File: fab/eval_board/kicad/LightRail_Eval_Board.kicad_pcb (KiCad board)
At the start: 22 copper layers, 100 x 100 mm, 191 parts, among them J1 Barrel_Jack, J10 SMA_RF4, J11 MPO_Fiber, J2 USB-C, J3 2-pin_Power, J5 JTAG_2x5, J6 GPIO_2x7, J7 SMA_RF1, J8 SMA_RF2, J9 SMA_RF3, SW1 Reset, U1 NCE_TEST_CHIP, U10 ADP7118-0.9V, U11 TPS7A20-1.8V, U12 TPS7A20-1.0V, U13 TPS7A33-3.3V, U14 TPS7A20-1.8V, U15 TPS54360, U2 XC7A100T, U20 Si5395A, U21 AD7928, U22 FT232H, U23 W25Q128JVS, U24 AD5684R, U25 TMP461, U3 TFLN_PIC, Y1 100MHz_TCXO

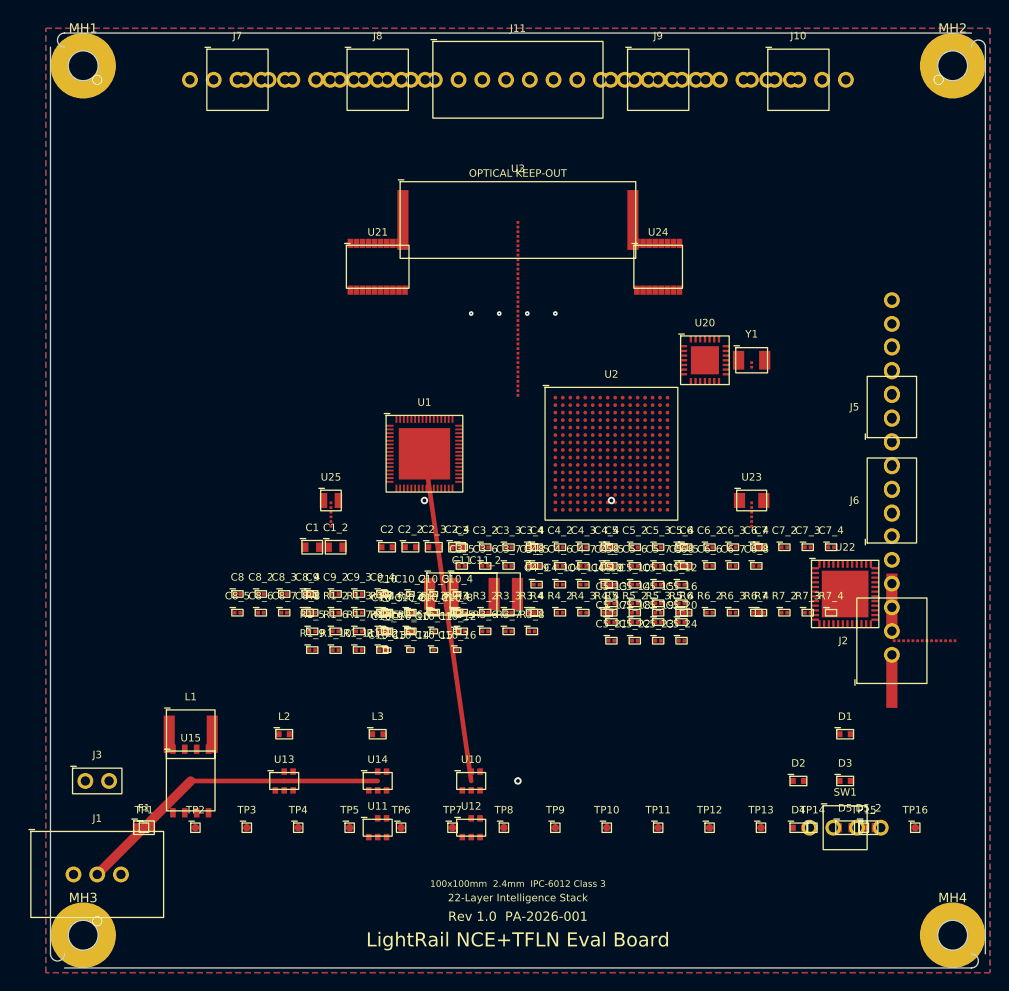
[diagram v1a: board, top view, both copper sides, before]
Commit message: feat: fully routed eval board PCB — 198 tracks, 118 vias, 11 filled zones, 40 Gerber files
- Deterministic signal router connects 75 signal nets across 6 copper layers
- GND/power planes via 11 copper zones (6 GND ref + 3 power + F.Cu/B.Cu GND)
- 22-layer Intelligence Stack: 100x100mm, 2.4mm thick, Megtron-7
- Gerber X2 + Excellon drill exported for all 22 Cu layers + non-copper
- Design rules: 0.1mm min clearance, 0.15mm trace, 0.3mm via drill
- Components: NCE QFN-64, Artix-7 BGA-256, TFLN MPO-24, TPS54360 buck, LDOs

Co-Authored-By: Bola Olatunji <bola.olatunji@ai.lightos.sh>
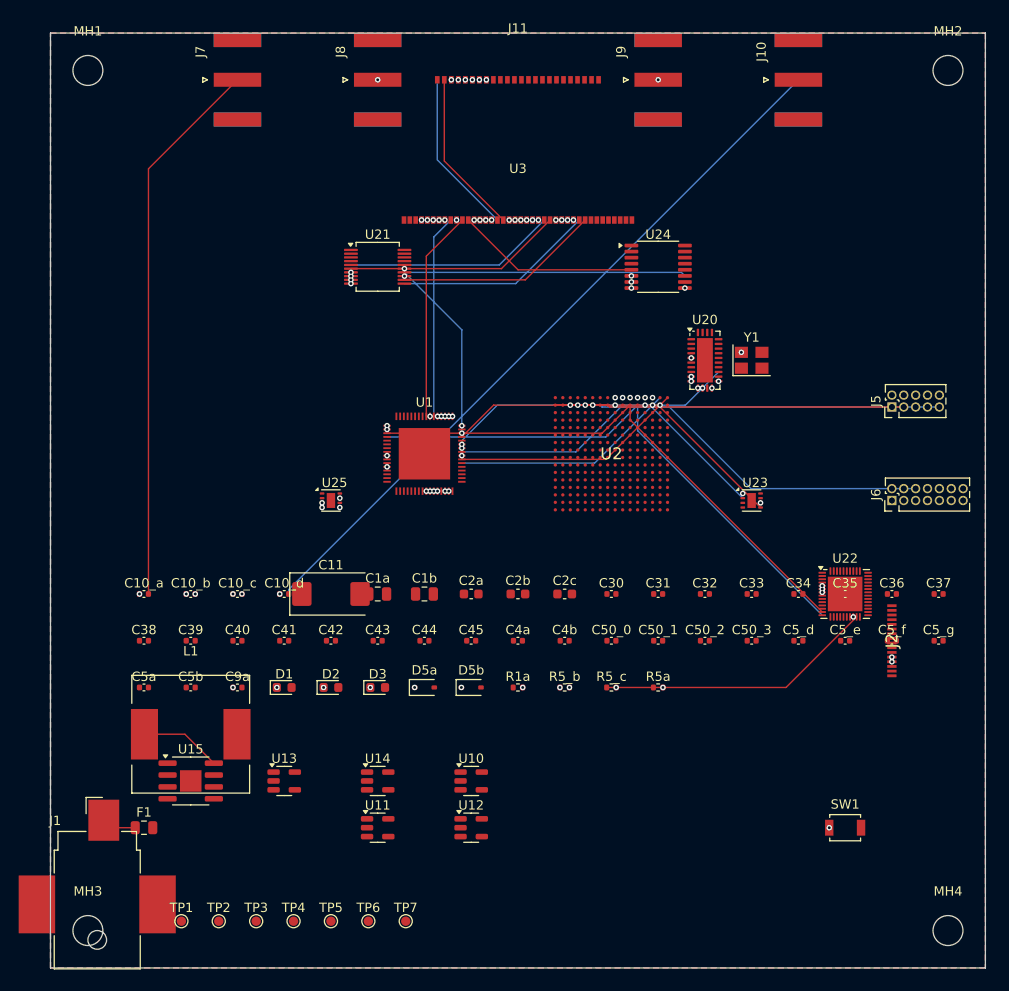
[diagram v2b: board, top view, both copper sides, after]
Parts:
- removed C1, C1_2: 22uF, LightRail:0805
- removed C10, C10_10, C10_11, C10_12, C10_13, C10_14, C10_15, C10_16, C10_2, C10_3, C10_4, C10_5, C10_6, C10_7, C10_8, C10_9: 100nF_AC, LightRail:0201
- removed C11_2: 100uF_Tant, LightRail:D_7343
- removed C2, C2_2, C2_3, C2_4: 10uF, LightRail:0603
- removed C3, C3_2, C3_3, C3_4, C3_5, C3_6, C3_7, C3_8: 4.7uF, LightRail:0402
- removed C4, C4_10, C4_11, C4_12, C4_2, C4_3, C4_4, C4_5, C4_6, C4_7, C4_8, C4_9: 1uF, LightRail:0402
- removed C5, C5_10, C5_11, C5_12, C5_13, C5_14, C5_15, C5_16, C5_17, C5_18, C5_19, C5_2, C5_20, C5_21, C5_22, C5_23, C5_24, C5_3, C5_4, C5_5, C5_6, C5_7, C5_8, C5_9: 100nF, LightRail:0402
- removed C6, C6_2, C6_3, C6_4, C6_5, C6_6, C6_7, C6_8: 10nF, LightRail:0402
- removed C7, C7_2, C7_3, C7_4: 1nF, LightRail:0402
- removed C8, C8_2, C8_3, C8_4, C8_5, C8_6, C8_7, C8_8: 100pF, LightRail:0402
- removed C9, C9_2, C9_3, C9_4: 22pF, LightRail:0402
- removed D4: LED_Yellow, LightRail:0603
- removed D5, D5_2: ESD_Diode, LightRail:SOD-323
- removed J3: 2-pin_Power, LightRail:PinHeader_1x02_P2.54mm
- removed L2, L3: Ferrite_Bead, LightRail:0603
- removed R1, R1_10, R1_11, R1_12, R1_2, R1_3, R1_4, R1_5, R1_6, R1_7, R1_8, R1_9: 10k, LightRail:0402
- removed R2, R2_2, R2_3, R2_4, R2_5, R2_6: 4.7k, LightRail:0402
- removed R3, R3_2, R3_3, R3_4, R3_5, R3_6, R3_7, R3_8: 100, LightRail:0402
- removed R4, R4_2, R4_3, R4_4: 49.9, LightRail:0402
- removed R5, R5_2, R5_3, R5_4: 330, LightRail:0402
- removed R6, R6_2, R6_3, R6_4: 0, LightRail:0402
- removed R7, R7_2, R7_3, R7_4: 1k, LightRail:0402
- removed TP10, TP11, TP12, TP13, TP14, TP15, TP16, TP8, TP9: Test_Point, LightRail:TP_0.8mm
- added C10_a: 100nF, C_0402_1005Metric, F.Cu at (110.0, 160.0)
- added C10_b: 100nF, C_0402_1005Metric, F.Cu at (115.0, 160.0)
- added C10_c: 100nF, C_0402_1005Metric, F.Cu at (120.0, 160.0)
- added C10_d: 100nF, C_0402_1005Metric, F.Cu at (125.0, 160.0)
- added C1a: 22uF, C_0805_2012Metric, F.Cu at (135.0, 160.0)
- added C1b: 22uF, C_0805_2012Metric, F.Cu at (140.0, 160.0)
- added C2a: 10uF, C_0603_1608Metric, F.Cu at (145.0, 160.0)
- added C2b: 10uF, C_0603_1608Metric, F.Cu at (150.0, 160.0)
- added C2c: 10uF, C_0603_1608Metric, F.Cu at (155.0, 160.0)
- added C30: 100nF, C_0402_1005Metric, F.Cu at (160.0, 160.0)
- added C31: 100nF, C_0402_1005Metric, F.Cu at (165.0, 160.0)
- added C32: 100nF, C_0402_1005Metric, F.Cu at (170.0, 160.0)
- added C33: 100nF, C_0402_1005Metric, F.Cu at (175.0, 160.0)
- added C34: 100nF, C_0402_1005Metric, F.Cu at (180.0, 160.0)
- added C35: 100nF, C_0402_1005Metric, F.Cu at (185.0, 160.0)
- added C36: 100nF, C_0402_1005Metric, F.Cu at (190.0, 160.0)
- added C37: 100nF, C_0402_1005Metric, F.Cu at (195.0, 160.0)
- added C38: 4.7uF, C_0402_1005Metric, F.Cu at (110.0, 165.0)
- added C39: 4.7uF, C_0402_1005Metric, F.Cu at (115.0, 165.0)
- added C40: 4.7uF, C_0402_1005Metric, F.Cu at (120.0, 165.0)
- added C41: 4.7uF, C_0402_1005Metric, F.Cu at (125.0, 165.0)
- added C42: 100nF, C_0402_1005Metric, F.Cu at (130.0, 165.0)
- added C43: 100nF, C_0402_1005Metric, F.Cu at (135.0, 165.0)
- added C44: 100nF, C_0402_1005Metric, F.Cu at (140.0, 165.0)
- added C45: 100nF, C_0402_1005Metric, F.Cu at (145.0, 165.0)
- added C4a: 1uF, C_0402_1005Metric, F.Cu at (150.0, 165.0)
- added C4b: 1uF, C_0402_1005Metric, F.Cu at (155.0, 165.0)
- added C50_0: 100nF, C_0402_1005Metric, F.Cu at (160.0, 165.0)
- added C50_1: 100nF, C_0402_1005Metric, F.Cu at (165.0, 165.0)
- added C50_2: 100nF, C_0402_1005Metric, F.Cu at (170.0, 165.0)
- added C50_3: 100nF, C_0402_1005Metric, F.Cu at (175.0, 165.0)
- added C5_d: 100nF, C_0402_1005Metric, F.Cu at (180.0, 165.0)
- added C5_e: 100nF, C_0402_1005Metric, F.Cu at (185.0, 165.0)
- added C5_f: 100nF, C_0402_1005Metric, F.Cu at (190.0, 165.0)
- added C5_g: 100nF, C_0402_1005Metric, F.Cu at (195.0, 165.0)
- added C5a: 100nF, C_0402_1005Metric, F.Cu at (110.0, 170.0)
- added C5b: 100nF, C_0402_1005Metric, F.Cu at (115.0, 170.0)
- added C9a: 100nF, C_0402_1005Metric, F.Cu at (120.0, 170.0)
- added D5a: PRTR5V0U2X, D_SOD-323, F.Cu at (140.0, 170.0)
- added D5b: PRTR5V0U2X, D_SOD-323, F.Cu at (145.0, 170.0)
- added R1a: 10k, R_0402_1005Metric, F.Cu at (150.0, 170.0)
- added R5_b: 330, R_0402_1005Metric, F.Cu at (155.0, 170.0)
- added R5_c: 330, R_0402_1005Metric, F.Cu at (160.0, 170.0)
- added R5a: 330, R_0402_1005Metric, F.Cu at (165.0, 170.0)
- C11: value 100uF_Tant -> 100uF; footprint LightRail:D_7343 -> CP_EIA-7343-15_Kemet-W
- D1: value LED_Green -> Green; footprint LightRail:0603 -> LED_0603_1608Metric
- D2: value LED_Blue -> Blue; footprint LightRail:0603 -> LED_0603_1608Metric
- D3: value LED_Red -> Red; footprint LightRail:0603 -> LED_0603_1608Metric
- F1: value Fuse_2A -> 2A; footprint LightRail:0805 -> Fuse_0805_2012Metric
- J1: value Barrel_Jack -> DC_12V; footprint LightRail:PJ-002AH -> BarrelJack_CUI_PJ-036AH-SMT_Horizontal
- J10: value SMA_RF4 -> SMA; footprint LightRail:SMA_Edge -> SMA_Amphenol_132289_EdgeMount
- J11: value MPO_Fiber -> MPO-24; footprint LightRail:MPO-24 -> MPO-24
- J2: footprint LightRail:USB_C_16pin -> LightRail:USB_C_Numeric
- J5: value JTAG_2x5 -> JTAG; footprint LightRail:PinHeader_2x05_P1.27mm -> PinHeader_2x05_P1.27mm_Vertical
- J6: value GPIO_2x7 -> GPIO; footprint LightRail:PinHeader_2x07_P1.27mm -> PinHeader_2x07_P1.27mm_Vertical
- J7: value SMA_RF1 -> SMA; footprint LightRail:SMA_Edge -> SMA_Amphenol_132289_EdgeMount
- J8: value SMA_RF2 -> SMA; footprint LightRail:SMA_Edge -> SMA_Amphenol_132289_EdgeMount
- J9: value SMA_RF3 -> SMA; footprint LightRail:SMA_Edge -> SMA_Amphenol_132289_EdgeMount
- L1: footprint LightRail:IND_5x5mm -> L_12x12mm_H4.5mm
- MH1, MH2, MH3, MH4: value MountingHole_M3 -> M3; footprint MountingHole:MountingHole_3.2mm_M3_Pad -> MountingHole_3.2mm_M3
- SW1: value Reset -> RESET; footprint LightRail:Tactile_4.5x4.5mm -> SW_SPST_B3U-1000P
- TP1: value Test_Point -> +12V; footprint LightRail:TP_0.8mm -> TestPoint_Pad_D1.0mm
- TP2: value Test_Point -> +5V; footprint LightRail:TP_0.8mm -> TestPoint_Pad_D1.0mm
- TP3: value Test_Point -> +3V3; footprint LightRail:TP_0.8mm -> TestPoint_Pad_D1.0mm
- TP4: value Test_Point -> +1V8; footprint LightRail:TP_0.8mm -> TestPoint_Pad_D1.0mm
- TP5: value Test_Point -> +1V0; footprint LightRail:TP_0.8mm -> TestPoint_Pad_D1.0mm
- TP6: value Test_Point -> +0V9; footprint LightRail:TP_0.8mm -> TestPoint_Pad_D1.0mm
- TP7: value Test_Point -> GND; footprint LightRail:TP_0.8mm -> TestPoint_Pad_D1.0mm
- U1: footprint LightRail:QFN-64_8x8mm_P0.4mm -> QFN-64_8x8mm_P0.4mm
- U10: value ADP7118-0.9V -> ADP7118; footprint LightRail:SOT-23-5 -> TSOT-23-5
- U11, U14: value TPS7A20-1.8V -> TPS7A2018; footprint LightRail:SOT-23-5 -> SOT-23-5
- U12: value TPS7A20-1.0V -> TPS7A2010; footprint LightRail:SOT-23-5 -> SOT-23-5
- U13: value TPS7A33-3.3V -> TPS7A3301; footprint LightRail:SOT-23-5 -> SOT-23-5
- U15: footprint LightRail:HSOP-8 -> HSOP-8-1EP_3.9x4.9mm_P1.27mm_EP2.3x2.3mm
- U2: footprint LightRail:BGA-256_14x14mm_P0.8mm -> LightRail:BGA-256_Numeric
- U20: footprint LightRail:QFN-28_5x5mm -> QFN-28-1EP_3x6mm_P0.5mm_EP1.7x4.75mm
- U21: footprint LightRail:TSSOP-20 -> TSSOP-20_4.4x5mm_P0.4mm
- U22: footprint LightRail:QFN-48_7x7mm -> QFN-48-1EP_5x5mm_P0.35mm_EP3.7x3.7mm
- U23: footprint LightRail:WSON-8_2x3mm -> WSON-8-1EP_2x2mm_P0.5mm_EP0.9x1.6mm
- U24: footprint LightRail:TSSOP-16 -> TSSOP-16_4.4x5mm_P0.65mm
- U25: footprint LightRail:WSON-8_2x2mm -> WSON-8-1EP_2x2mm_P0.5mm_EP0.9x1.6mm
- U3: footprint LightRail:Custom_Optical_Module -> Custom_Optical_Module
- Y1: value 100MHz_TCXO -> 100MHz; footprint LightRail:3.2x2.5mm -> Crystal_SMD_3225-4Pin_3.2x2.5mm
- moved D1 60.2 mm to (125.0, 170.0)
- moved D2 51.0 mm to (130.0, 170.0)
- moved D3 51.0 mm to (135.0, 170.0)
- moved C11 14.0 mm to (130.0, 160.0)
- moved TP7 11.2 mm to (138.0, 195.0)
- moved TP1 10.8 mm to (114.0, 195.0)
- moved TP6 10.6 mm to (134.0, 195.0)
- moved TP2 10.3 mm to (118.0, 195.0)
- moved TP5 10.2 mm to (130.0, 195.0)
- moved TP3 10.0 mm to (122.0, 195.0)
- moved TP4 10.0 mm to (126.0, 195.0)
- moved MH1 0.71 mm to (104.0, 104.0)
- moved MH2 0.71 mm to (196.0, 104.0)
- moved MH3 0.71 mm to (104.0, 196.0)
- moved MH4 0.71 mm to (196.0, 196.0)
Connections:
- net net_J2_1 renamed +5V_USB
- net net_J5_10 renamed JTAG_TRST
- net net_U10_5 renamed NR_0V9
- net net_U11_3 renamed NR_1V8
- net net_U12_3 renamed NR_1V0
- net net_U13_3 renamed NR_3V3
- net net_U14_3 renamed NR_1V8F
- net net_U15_1 renamed BOOT_5V
- net net_U15_5 renamed FB_5V
- net net_U15_6 renamed COMP_5V
- net net_U1_13 renamed AXI_AWREADY
- net net_U1_16 renamed AXI_WREADY
- net net_U1_17 renamed AXI_BRESP
- net net_U1_18 renamed AXI_BVALID
- net net_U1_19 renamed AXI_ARADDR
- net net_U1_20 renamed AXI_ARVALID
- net net_U1_21 renamed AXI_ARREADY
- net net_U1_41 renamed HBM_DQ0
- net net_U1_42 renamed HBM_DQ1
- net net_U1_43 renamed HBM_DQ2
- net net_U1_44 renamed HBM_DQ3
- net net_U1_45 renamed HBM_DQ4
- net net_U1_46 renamed HBM_DQ5
- net net_U1_47 renamed HBM_DQ6
- net net_U1_48 renamed HBM_DQ7
- net net_U1_53 renamed NCE_GPIO0
- net net_U1_54 renamed NCE_GPIO1
- net net_U1_55 renamed NCE_GPIO2
- net net_U1_56 renamed NCE_GPIO3
- net net_U1_58 renamed NCE_PG
- net net_U1_59 renamed NCE_STATUS
- net net_U20_16 renamed CLK_CORE_N
- net net_U20_18 renamed CLK_REF_N
- net net_U20_19 renamed CLK_SERDES
- net net_U20_20 renamed CLK_SERDES_N
- net net_U20_22 renamed CLK_HBM_N
- net net_U20_23 renamed CLK_100M_BUF
- net net_U20_24 renamed CLK_100M_BUF_N
- net net_U21_16 renamed SPI_CS_ADC
- net net_U22_11 renamed CLK_12M
- net net_U22_12 renamed CLK_12M_OUT
- net net_U22_15 renamed UART_RTS
- net net_U22_16 renamed UART_CTS
- net net_U22_21 renamed FT_PWREN
- net net_U24_10 renamed SPI_CS_DAC
- C11 pad 1: net_C11_1 -> +12V
- C11 pad 2: net_C11_2 -> GND
- D1 pad 1: net_D1_1 -> LED_A
- D1 pad 2: net_D1_2 -> GND
- D2 pad 1: net_D2_1 -> LED_D2
- D2 pad 2: net_D2_2 -> GND
- D3 pad 1: net_D3_1 -> LED_D3
- D3 pad 2: net_D3_2 -> GND
- F1 pad 1: net_F1_1 -> +12V_RAW
- F1 pad 2: net_F1_2 -> +12V
- J1 pad 1: net_J1_1 -> +12V_RAW
- J1 pad 2: net_J1_2 -> GND
- J1 pad 3: net_J1_3 -> (no net)
- J10 pad 1: net_J10_1 -> SMA_J10
- J10 pad 2: net_J10_2 -> GND
- J11 pad 1: net_J11_1 -> OPT_TX0
- J11 pad 10: net_J11_10 -> (no net)
- J11 pad 11: net_J11_11 -> (no net)
- J11 pad 12: net_J11_12 -> (no net)
- J11 pad 13: net_J11_13 -> (no net)
- J11 pad 14: net_J11_14 -> (no net)
- J11 pad 15: net_J11_15 -> (no net)
- J11 pad 16: net_J11_16 -> (no net)
- J11 pad 17: net_J11_17 -> (no net)
- J11 pad 18: net_J11_18 -> (no net)
- J11 pad 19: net_J11_19 -> (no net)
- J11 pad 2: net_J11_2 -> OPT_TX1
- J11 pad 20: net_J11_20 -> (no net)
- J11 pad 21: net_J11_21 -> (no net)
- J11 pad 22: net_J11_22 -> (no net)
- J11 pad 23: net_J11_23 -> (no net)
- J11 pad 24: net_J11_24 -> (no net)
- J11 pad 3: net_J11_3 -> OPT_TX2
- J11 pad 4: net_J11_4 -> OPT_TX3
- J11 pad 5: net_J11_5 -> OPT_RX0
- J11 pad 6: net_J11_6 -> OPT_RX1
- J11 pad 7: net_J11_7 -> OPT_RX2
- J11 pad 8: net_J11_8 -> OPT_RX3
- J11 pad 9: net_J11_9 -> (no net)
- J2 pad 10: net_J2_10 -> (no net)
- J2 pad 11: net_J2_11 -> (no net)
- J2 pad 12: net_J2_12 -> (no net)
- J2 pad 13: net_J2_13 -> (no net)
- J2 pad 14: net_J2_14 -> (no net)
- J2 pad 15: net_J2_15 -> (no net)
- J2 pad 16: net_J2_16 -> (no net)
- J2 pad 2: net_J2_2 -> (no net)
- J2 pad 3: net_J2_3 -> (no net)
- J2 pad 4: net_J2_4 -> USB_DP
- J2 pad 5: net_J2_5 -> USB_DN
- J2 pad 6: net_J2_6 -> (no net)
- J2 pad 7: net_J2_7 -> (no net)
- J2 pad 8: net_J2_8 -> GND
- J2 pad 9: net_J2_9 -> GND
- J5 pad 1: net_J5_1 -> JTAG_TCK
- J5 pad 2: net_J5_2 -> GND
- J5 pad 3: net_J5_3 -> JTAG_TDO
- J5 pad 4: net_J5_4 -> +3V3
- J5 pad 5: net_J5_5 -> JTAG_TMS
- J5 pad 6: net_J5_6 -> GND
- J5 pad 7: net_J5_7 -> (no net)
- J5 pad 8: net_J5_8 -> (no net)
- J5 pad 9: net_J5_9 -> JTAG_TDI
- J6 pad 1: net_J6_1 -> +3V3
- J6 pad 10: net_J6_10 -> (no net)
- J6 pad 11: net_J6_11 -> (no net)
- J6 pad 12: net_J6_12 -> (no net)
- J6 pad 13: net_J6_13 -> I2C_SCL
- J6 pad 14: net_J6_14 -> I2C_SDA
- J6 pad 2: net_J6_2 -> GND
- J6 pad 3: net_J6_3 -> FPGA_GPIO0
- J6 pad 4: net_J6_4 -> FPGA_GPIO1
- J6 pad 5: net_J6_5 -> FPGA_GPIO2
- J6 pad 6: net_J6_6 -> FPGA_GPIO3
- J6 pad 7: net_J6_7 -> (no net)
- J6 pad 8: net_J6_8 -> (no net)
- J6 pad 9: net_J6_9 -> (no net)
- J7 pad 1: net_J7_1 -> SMA_J7
- J7 pad 2: net_J7_2 -> GND
- J8 pad 1: net_J8_1 -> SMA_J8
- J8 pad 2: net_J8_2 -> GND
- J9 pad 1: net_J9_1 -> SMA_J9
- J9 pad 2: net_J9_2 -> GND
- L1 pad 1: net_L1_1 -> SW_5V
- L1 pad 2: net_L1_2 -> +5V
- SW1 pad 1: net_SW1_1 -> RESET_N
- SW1 pad 2: net_SW1_2 -> GND
- TP1 pad 1: net_TP1_1 -> +12V
- TP2 pad 1: net_TP2_1 -> +5V
- TP3 pad 1: net_TP3_1 -> +3V3
- TP4 pad 1: net_TP4_1 -> +1V8
- TP5 pad 1: net_TP5_1 -> +1V0
- TP6 pad 1: net_TP6_1 -> +0V9
- TP7 pad 1: net_TP7_1 -> GND
- U1 pad 1: net_U1_1 -> +0V9
- U1 pad 10: net_U1_10 -> AXI_ARESETN
- U1 pad 11: net_U1_11 -> AXI_AWADDR
- U1 pad 12: net_U1_12 -> AXI_AWVALID
- U1 pad 14: net_U1_14 -> AXI_WDATA
- U1 pad 15: net_U1_15 -> AXI_WVALID
- U1 pad 2: net_U1_2 -> +0V9
- U1 pad 22: net_U1_22 -> AXI_RDATA
- U1 pad 23: net_U1_23 -> AXI_RVALID
- U1 pad 24: net_U1_24 -> CLK_CORE
- U1 pad 25: net_U1_25 -> CLK_REF
- U1 pad 26: net_U1_26 -> JTAG_TCK
- U1 pad 27: net_U1_27 -> JTAG_TMS
- U1 pad 28: net_U1_28 -> JTAG_TDI
- U1 pad 29: net_U1_29 -> JTAG_TDO
- U1 pad 3: net_U1_3 -> +1V8
- U1 pad 30: net_U1_30 -> SPI_CLK
- U1 pad 31: net_U1_31 -> SPI_MOSI
- U1 pad 32: net_U1_32 -> SPI_MISO
- U1 pad 33: net_U1_33 -> TFLN_TX_P0
- U1 pad 34: net_U1_34 -> TFLN_TX_N0
- U1 pad 35: net_U1_35 -> TFLN_TX_P1
- U1 pad 36: net_U1_36 -> TFLN_TX_N1
- U1 pad 37: net_U1_37 -> TFLN_TX_P2
- U1 pad 38: net_U1_38 -> TFLN_TX_N2
- U1 pad 39: net_U1_39 -> TFLN_TX_P3
- U1 pad 4: net_U1_4 -> +1V8
- U1 pad 40: net_U1_40 -> TFLN_TX_N3
- U1 pad 49: net_U1_49 -> I2C_SCL
- U1 pad 5: net_U1_5 -> GND
- U1 pad 50: net_U1_50 -> I2C_SDA
- U1 pad 51: net_U1_51 -> UART_TX
- U1 pad 52: net_U1_52 -> UART_RX
- U1 pad 57: net_U1_57 -> TEMP_ALERT
- U1 pad 6: net_U1_6 -> GND
- U1 pad 60: net_U1_60 -> RESET_N
- U1 pad 61: net_U1_61 -> GND
- U1 pad 62: net_U1_62 -> GND
- U1 pad 63: net_U1_63 -> +0V9
- U1 pad 64: net_U1_64 -> +1V8
- U1 pad 65: GND -> (no net)
- U1 pad 7: net_U1_7 -> GND
- U1 pad 8: net_U1_8 -> GND
- U1 pad 9: net_U1_9 -> AXI_ACLK
- U10 pad 1: net_U10_1 -> +1V8
- U10 pad 2: net_U10_2 -> +1V8
- U10 pad 3: net_U10_3 -> GND
- U10 pad 4: net_U10_4 -> +0V9
- U11 pad 1: net_U11_1 -> +3V3
- U11 pad 2: net_U11_2 -> +3V3
- U11 pad 4: net_U11_4 -> +1V8
- U11 pad 5: net_U11_5 -> GND
- U12 pad 1: net_U12_1 -> +1V8
- U12 pad 2: net_U12_2 -> +1V8
- U12 pad 4: net_U12_4 -> +1V0
- U12 pad 5: net_U12_5 -> GND
- U13 pad 1: net_U13_1 -> +5V
- U13 pad 2: net_U13_2 -> +5V
- U13 pad 4: net_U13_4 -> +3V3
- U13 pad 5: net_U13_5 -> GND
- U14 pad 1: net_U14_1 -> +3V3
- U14 pad 2: net_U14_2 -> +3V3
- U14 pad 4: net_U14_4 -> +1V8
- U14 pad 5: net_U14_5 -> GND
- U15 pad 2: net_U15_2 -> +12V
- U15 pad 3: net_U15_3 -> +12V
- U15 pad 4: net_U15_4 -> GND
- U15 pad 7: net_U15_7 -> GND
- U15 pad 8: net_U15_8 -> SW_5V
- U20 pad 1: net_U20_1 -> +3V3
- U20 pad 10: net_U20_10 -> I2C_SCL
- U20 pad 11: net_U20_11 -> RESET_N
- U20 pad 12: net_U20_12 -> PLL_LOL
- U20 pad 13: net_U20_13 -> +3V3
- U20 pad 14: net_U20_14 -> PLL_LOL
- U20 pad 15: net_U20_15 -> CLK_CORE
- U20 pad 17: net_U20_17 -> CLK_REF
- U20 pad 2: net_U20_2 -> +1V8
- U20 pad 21: net_U20_21 -> CLK_HBM
- U20 pad 25: net_U20_25 -> +1V8
- U20 pad 26: net_U20_26 -> +1V8
- U20 pad 27: net_U20_27 -> +1V8
- U20 pad 28: net_U20_28 -> GND
- U20 pad 29: GND -> (no net)
- U20 pad 3: net_U20_3 -> GND
- U20 pad 4: net_U20_4 -> GND
- U20 pad 5: net_U20_5 -> CLK_100M
- U20 pad 6: net_U20_6 -> GND
- U20 pad 7: net_U20_7 -> GND
- U20 pad 8: net_U20_8 -> GND
- U20 pad 9: net_U20_9 -> I2C_SDA
- U21 pad 1: net_U21_1 -> +3V3
- U21 pad 10: net_U21_10 -> MON_CH5
- U21 pad 11: net_U21_11 -> MON_CH6
- U21 pad 12: net_U21_12 -> MON_CH7
- U21 pad 13: net_U21_13 -> SPI_CLK
- U21 pad 14: net_U21_14 -> SPI_MOSI
- U21 pad 15: net_U21_15 -> SPI_MISO
- U21 pad 17: net_U21_17 -> +3V3
- U21 pad 18: net_U21_18 -> GND
- U21 pad 19: net_U21_19 -> (no net)
- U21 pad 2: net_U21_2 -> +3V3
- U21 pad 20: net_U21_20 -> (no net)
- U21 pad 3: net_U21_3 -> GND
- U21 pad 4: net_U21_4 -> GND
- U21 pad 5: net_U21_5 -> MON_CH0
- U21 pad 6: net_U21_6 -> MON_CH1
- U21 pad 7: net_U21_7 -> MON_CH2
- U21 pad 8: net_U21_8 -> MON_CH3
- U21 pad 9: net_U21_9 -> MON_CH4
- U22 pad 1: net_U22_1 -> +3V3
- U22 pad 10: net_U22_10 -> (no net)
- U22 pad 13: net_U22_13 -> UART_TX
- U22 pad 14: net_U22_14 -> UART_RX
- U22 pad 17: net_U22_17 -> (no net)
- U22 pad 18: net_U22_18 -> (no net)
- U22 pad 19: net_U22_19 -> (no net)
- U22 pad 2: net_U22_2 -> +3V3
- U22 pad 20: net_U22_20 -> (no net)
- U22 pad 22: net_U22_22 -> FT_TXLED
- U22 pad 23: net_U22_23 -> FT_RXLED
- U22 pad 24: net_U22_24 -> (no net)
- U22 pad 25: net_U22_25 -> (no net)
- U22 pad 26: net_U22_26 -> (no net)
- U22 pad 27: net_U22_27 -> (no net)
- U22 pad 28: net_U22_28 -> (no net)
- U22 pad 29: net_U22_29 -> (no net)
- U22 pad 3: net_U22_3 -> GND
- U22 pad 30: net_U22_30 -> (no net)
- U22 pad 31: net_U22_31 -> (no net)
- U22 pad 32: net_U22_32 -> (no net)
- U22 pad 33: net_U22_33 -> (no net)
- U22 pad 34: net_U22_34 -> (no net)
- U22 pad 35: net_U22_35 -> (no net)
- U22 pad 36: net_U22_36 -> (no net)
- U22 pad 37: net_U22_37 -> (no net)
- U22 pad 38: net_U22_38 -> (no net)
- U22 pad 39: net_U22_39 -> (no net)
- U22 pad 4: net_U22_4 -> GND
- U22 pad 40: net_U22_40 -> (no net)
- U22 pad 41: net_U22_41 -> (no net)
- U22 pad 42: net_U22_42 -> (no net)
- U22 pad 43: net_U22_43 -> (no net)
- U22 pad 44: net_U22_44 -> (no net)
- U22 pad 45: net_U22_45 -> (no net)
- U22 pad 46: net_U22_46 -> (no net)
- U22 pad 47: net_U22_47 -> (no net)
- U22 pad 48: net_U22_48 -> (no net)
- U22 pad 49: GND -> (no net)
- U22 pad 5: net_U22_5 -> USB_DP
- U22 pad 6: net_U22_6 -> USB_DN
- U22 pad 7: net_U22_7 -> RESET_N
- U22 pad 8: net_U22_8 -> (no net)
- U22 pad 9: net_U22_9 -> (no net)
- U23 pad 1: net_U23_1 -> FLASH_CS
- U23 pad 2: net_U23_2 -> FLASH_MISO
- U23 pad 3: net_U23_3 -> +3V3
- U23 pad 4: net_U23_4 -> GND
- U23 pad 5: net_U23_5 -> FLASH_MOSI
- U23 pad 6: net_U23_6 -> FLASH_SCK
- U23 pad 7: net_U23_7 -> +3V3
- U23 pad 8: net_U23_8 -> +3V3
- U24 pad 1: net_U24_1 -> +3V3
- U24 pad 11: net_U24_11 -> SPI_MOSI
- U24 pad 12: net_U24_12 -> GND
- U24 pad 13: net_U24_13 -> +3V3
- U24 pad 14: net_U24_14 -> +3V3
- U24 pad 15: net_U24_15 -> (no net)
- U24 pad 16: net_U24_16 -> (no net)
- U24 pad 2: net_U24_2 -> +3V3
- U24 pad 3: net_U24_3 -> GND
- U24 pad 4: net_U24_4 -> GND
- U24 pad 5: net_U24_5 -> DAC_V1
- U24 pad 6: net_U24_6 -> DAC_V2
- U24 pad 7: net_U24_7 -> DAC_V3
- U24 pad 8: net_U24_8 -> DAC_V4
- U24 pad 9: net_U24_9 -> SPI_CLK
- U25 pad 1: net_U25_1 -> +3V3
- U25 pad 2: net_U25_2 -> GND
- U25 pad 3: net_U25_3 -> I2C_SDA
- U25 pad 4: net_U25_4 -> I2C_SCL
- U25 pad 5: net_U25_5 -> TEMP_ALERT
- U25 pad 6: net_U25_6 -> GND
- U25 pad 7: net_U25_7 -> TEMP_DIODE
- U25 pad 8: net_U25_8 -> GND
- U3 pad 1: net_U3_1 -> +1V8
- U3 pad 10: net_U3_10 -> TFLN_TX_P3
- U3 pad 11: net_U3_11 -> TFLN_TX_N3
- U3 pad 12: net_U3_12 -> DAC_V1
- U3 pad 13: net_U3_13 -> DAC_V2
- U3 pad 14: net_U3_14 -> DAC_V3
- U3 pad 15: net_U3_15 -> DAC_V4
- U3 pad 16: net_U3_16 -> TEMP_DIODE
- U3 pad 17: net_U3_17 -> OPT_TX0
- U3 pad 18: net_U3_18 -> OPT_TX1
- U3 pad 19: net_U3_19 -> OPT_TX2
- U3 pad 2: net_U3_2 -> GND
- U3 pad 20: net_U3_20 -> OPT_TX3
- U3 pad 21: net_U3_21 -> OPT_RX0
- U3 pad 22: net_U3_22 -> OPT_RX1
- U3 pad 23: net_U3_23 -> OPT_RX2
- U3 pad 24: net_U3_24 -> OPT_RX3
- U3 pad 25: net_U3_25 -> MON_CH0
- U3 pad 26: net_U3_26 -> MON_CH1
- U3 pad 27: net_U3_27 -> MON_CH2
- U3 pad 28: net_U3_28 -> MON_CH3
- U3 pad 29: net_U3_29 -> MON_CH4
- U3 pad 3: net_U3_3 -> GND
- U3 pad 30: net_U3_30 -> MON_CH5
- U3 pad 31: net_U3_31 -> MON_CH6
- U3 pad 32: net_U3_32 -> MON_CH7
- U3 pad 33: net_U3_33 -> (no net)
- U3 pad 34: net_U3_34 -> (no net)
- U3 pad 35: net_U3_35 -> (no net)
- U3 pad 36: net_U3_36 -> (no net)
- U3 pad 37: net_U3_37 -> (no net)
- U3 pad 38: net_U3_38 -> (no net)
- U3 pad 39: net_U3_39 -> (no net)
- U3 pad 4: net_U3_4 -> TFLN_TX_P0
- U3 pad 40: net_U3_40 -> (no net)
- U3 pad 5: net_U3_5 -> TFLN_TX_N0
- U3 pad 6: net_U3_6 -> TFLN_TX_P1
- U3 pad 7: net_U3_7 -> TFLN_TX_N1
- U3 pad 8: net_U3_8 -> TFLN_TX_P2
- U3 pad 9: net_U3_9 -> TFLN_TX_N2
- Y1 pad 1: net_Y1_1 -> +3V3
- Y1 pad 2: net_Y1_2 -> +3V3
- Y1 pad 3: net_Y1_3 -> GND
- Y1 pad 4: net_Y1_4 -> CLK_100M
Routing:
- net RESET_N: track 0.00 -> 174.6 mm, vias 0 -> 6
- net I2C_SCL: track 0.00 -> 80.5 mm, vias 0 -> 4
- net I2C_SDA: track 0.00 -> 79.7 mm, vias 0 -> 4
- net SMA_J10: track 0.00 -> 77.6 mm
- net SMA_J9: track 0.00 -> 73.4 mm, vias 0 -> 2
- net TFLN_TX_P0: track 0.00 -> 63.7 mm, vias 0 -> 3
- net SMA_J8: track 0.00 -> 63.1 mm, vias 0 -> 2
- net SMA_J7: track 0.00 -> 58.9 mm
- net UART_RX: track 0.00 -> 58.9 mm
- net TFLN_TX_N0: track 0.00 -> 57.9 mm, vias 0 -> 3
- net UART_TX: track 0.00 -> 57.9 mm
- net JTAG_TDI: track 0.00 -> 52.7 mm
- net USB_DP: track 7.07 -> 59.3 mm, vias 0 -> 3
- net TFLN_TX_P1: track 0.00 -> 52.1 mm, vias 0 -> 3
- net JTAG_TMS: track 0.00 -> 50.4 mm, vias 0 -> 3
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- added copper zone on In16.Cu, net +1V8
- removed copper zone on In16.Cu, net +1V0
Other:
- outline, holes or cut-outs redrawn
- rule pad_to_mask_clearance: 0.05 -> 0
- board text removed: "1. Material: Megtron-7 (outer), FR-4 High-Tg (inner)"
- board text removed: "100x100mm 2.4mm IPC-6012 Class 3"
- board text removed: "2. Finish: ENIG (Electroless Nickel Immersion Gold)"
- board text removed: "22-Layer Intelligence Stack"
- board text removed: "3. Min trace/space: 0.08mm/0.08mm"
- board text removed: "4. Min drill: 0.15mm (blind), 0.20mm (buried), 0.25mm (through)"
- board text removed: "5. Impedance: 50 ohm SE, 90 ohm diff (USB), 100 ohm diff (TFLN)"
- board text removed: "6. IPC-6012 Class 3"
- board text removed: "7. Back-drill TFLN RF vias to reduce stub length"
- board text removed: "8. Controlled impedance on layers: L1,L2,L4,L5,L20,L22"
- board text removed: "FAB NOTES:"
- board text removed: "LightRail NCE+TFLN Eval Board"
- board text removed: "OPTICAL KEEP-OUT"
- board text removed: "Rev 1.0 PA-2026-001"

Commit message: fix: add 7 net_class blocks to PCB file for DRC enforcement
Added net_class definitions (Default, AXI_BUS, CLK_2GHZ, TFLN_RF, USB_HS,
PWR_5V, PWR_CORE) directly to .kicad_pcb so KiCad 8 DRC can enforce
per-class track width and clearance rules.

Also updated .kicad_pro with net-to-class assignments for all known nets.

Co-Authored-By: Bola Olatunji <bola.olatunji@ai.lightos.sh>
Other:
- net class AXI_BUS added: clearance 0.15, trace_width 0.15, via_dia 0.6, via_drill 0.3
- net class CLK_2GHZ added: clearance 0.15, trace_width 0.12, via_dia 0.5, via_drill 0.25
- net class Default added: clearance 0.2, trace_width 0.2, via_dia 0.6, via_drill 0.3
- net class PWR_5V added: clearance 0.3, trace_width 0.5, via_dia 0.8, via_drill 0.4
- net class PWR_CORE added: clearance 0.25, trace_width 0.4, via_dia 0.8, via_drill 0.4
- net class TFLN_RF added: clearance 0.2, trace_width 0.1, via_dia 0.5, via_drill 0.25
- net class USB_HS added: clearance 0.15, trace_width 0.15, via_dia 0.6, via_drill 0.3
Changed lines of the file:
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@@
 		)
+	)
+	(net_class "Default" "Default net class"
+		(clearance 0.2)
+		(trace_width 0.2)
+		(via_dia 0.6)
+		(via_drill 0.3)
+		(uvia_dia 0.3)
+		(uvia_drill 0.1)
+		(diff_pair_width 0.2)
+		(diff_pair_gap 0.25)
+	)
+	(net_class "AXI_BUS" "AXI4-Lite bus signals — 100 ohm differential, length-matched"
+		(clearance 0.15)
+		(trace_width 0.15)
+		(via_dia 0.6)
+		(via_drill 0.3)
+		(uvia_dia 0.3)
+		(uvia_drill 0.1)
+		(diff_pair_width 0.15)
+		(diff_pair_gap 0.15)
+		(add_net "AXI_ACLK")
+		(add_net "AXI_ARADDR")
+		(add_net "AXI_ARESETN")
+		(add_net "AXI_ARREADY")
+		(add_net "AXI_ARVALID")
+		(add_net "AXI_AWADDR")
+		(add_net "AXI_AWREADY")
+		(add_net "AXI_AWVALID")
+		(add_net "AXI_BREADY")
+		(add_net "AXI_BRESP")
+		(add_net "AXI_BVALID")
+		(add_net "AXI_RDATA")
+		(add_net "AXI_RREADY")
+		(add_net "AXI_RRESP")
+		(add_net "AXI_RVALID")
+		(add_net "AXI_WDATA")
+		(add_net "AXI_WREADY")
+		(add_net "AXI_WSTRB")
+		(add_net "AXI_WVALID")
+	)
+	(net_class "CLK_2GHZ" "High-speed clock distribution — tight clearance, matched length"
+		(clearance 0.15)
+		(trace_width 0.12)
+		(via_dia 0.5)
+		(via_drill 0.25)
+		(uvia_dia 0.3)
+		(uvia_drill 0.1)
+		(diff_pair_width 0.12)
+		(diff_pair_gap 0.12)
+		(add_net "CLK_200MHZ")
+		(add_net "CLK_200MHZ_N")
+		(add_net "CLK_REF_50M")
+		(add_net "CLK_FPGA")
+	)
+	(net_class "TFLN_RF" "TFLN optical engine RF pairs — 100 ohm diff, controlled impedance"
+		(clearance 0.2)
+		(trace_width 0.1)
+		(via_dia 0.5)
+		(via_drill 0.25)
+		(uvia_dia 0.3)
+		(uvia_drill 0.1)
+		(diff_pair_width 0.1)
+		(diff_pair_gap 0.14)
+		(add_net "TFLN_TX_P0")
+		(add_net "TFLN_TX_P1")
+		(add_net "TFLN_TX_P2")
+		(add_net "TFLN_TX_P3")
+		(add_net "TFLN_TX_P4")
+		(add_net "TFLN_TX_P5")
+		(add_net "TFLN_TX_P6")
+		(add_net "TFLN_TX_P7")
+		(add_net "TFLN_RX_P0")
+		(add_net "TFLN_RX_P1")
+		(add_net "TFLN_RX_P2")
+		(add_net "TFLN_RX_P3")
+		(add_net "RF_PROBE_P")
+		(add_net "RF_PROBE_N")
+	)
+	(net_class "USB_HS" "USB 2.0 High-Speed — 90 ohm differential pair"
+		(clearance 0.15)
+		(trace_width 0.15)
+		(via_dia 0.6)
+		(via_drill 0.3)
+		(uvia_dia 0.3)
+		(uvia_drill 0.1)
+		(diff_pair_width 0.15)
+		(diff_pair_gap 0.15)
+		(add_net "USB_D_P")
+		(add_net "USB_D_N")
+	)
+	(net_class "PWR_5V" "5V/12V power distribution — wide traces, large vias"
+		(clearance 0.3)
+		(trace_width 0.5)
+		(via_dia 0.8)
+		(via_drill 0.4)
+		(uvia_dia 0.3)
+		(uvia_drill 0.1)
+		(diff_pair_width 0.5)
+		(diff_pair_gap 0.25)
+		(add_net "+5V")
+		(add_net "+5V_USB")
+		(add_net "+12V")
+		(add_net "+12V_RAW")
+	)
+	(net_class "PWR_CORE" "Core voltage power — 0.9V/1.0V/1.8V/3.3V rails"
+		(clearance 0.25)
+		(trace_width 0.4)
+		(via_dia 0.8)
+		(via_drill 0.4)
+		(uvia_dia 0.3)
+		(uvia_drill 0.1)
+		(diff_pair_width 0.4)
+		(diff_pair_gap 0.25)
+		(add_net "+0V9")
+		(add_net "+1V0")
+		(add_net "+1V8")
+		(add_net "+3V3")
 	)
 	(net 0 "")
